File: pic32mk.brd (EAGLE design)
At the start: 110.2 x 85.1 mm, 91 parts, among them IC1 PIC32MK1024MCF100-I_PT, IC10 5.0VDC, IC11 3.3VDC, IC2 ADM3095EBRZ, IC3 TXB0101DCKR, IC4 MAX203ECWP, IC5 TXB0101DCKR, IC6 TXB0101DCKR, IC7 TXB0101DCKR, IC8 TXB0101DCKR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

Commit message: up
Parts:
- added X3: 53261-10, con-molex:53261-10
- moved S1 5.39 mm to (91.4, 10.2)
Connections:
- new net D1+: IC1.57, X3.4
- new net D1-: IC1.56, X3.3
- new net D2+: IC1.60, X3.7
- new net D2-: IC1.59, X3.6
- new net USBID1: IC1.69, X3.1
- new net VBUS: IC1.54, X3.2
- new net VBUS2: IC1.58, X3.5
- net IN7: now also IC1.76; no longer IC1.69
- net SOSCI: now also SPI.10
- net VCC: now also X3.10
- net VDD: now also X3.9; no longer SPI.10
- net VSS: now also X3.8
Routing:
- net VDD: track 439.7 -> 344.6 mm, vias 11 -> 19
- net D2+: track 0.00 -> 70.2 mm, vias 0 -> 3
- net D2-: track 0.00 -> 68.4 mm, vias 0 -> 3
- net VBUS2: track 0.00 -> 63.4 mm, vias 0 -> 3
- net USBID1: track 0.00 -> 60.6 mm, vias 0 -> 2
- net D1-: track 0.00 -> 59.3 mm, vias 0 -> 2
- net D1+: track 0.00 -> 59.3 mm, vias 0 -> 3
- net VBUS: track 0.00 -> 54.8 mm, vias 0 -> 2
- net GND: track 137.7 -> 188.9 mm, vias 4 -> 2
- net RF13: track 96.0 -> 144.4 mm
- net PWM2H: track 86.2 -> 47.9 mm, vias 2 -> 3
- net +24V: track 199.8 -> 237.9 mm, vias 3 -> 5
- net SOSCI: track 0.00 -> 35.4 mm, vias 0 -> 1
- net PWM1L: track 71.6 -> 42.3 mm, vias 2 -> 3
- net RE8: track 62.2 -> 91.1 mm, vias 7 -> 3
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
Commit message: up
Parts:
- renumbered S1 to RESET, X1 to QEI, X3 to USB-BO
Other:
- board text added: "fgb@mchp vcan 1.06"
- board text removed: "fgb@mchp vcan 1.05"

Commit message: up
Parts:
- added QEI3: 22-23-2041, con-molex:22-23-2041
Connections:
- net RG6: now also QEI3.2
- net RG7: now also QEI3.1
- net VDD: now also QEI3.3
- net VSS: now also QEI3.4
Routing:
- net RG7: track 30.8 -> 54.0 mm
- net RG6: track 36.6 -> 50.6 mm
- net RE8: track 91.1 -> 97.3 mm
- net VDD: track 344.6 -> 348.0 mm
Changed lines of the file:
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@@
 <attribute name="VALUE" x="89.59" y="-0.77" size="1.27" layer="27" rot="R180"/>
 </element>
+<element name="QEI3" library="con-molex" library_urn="urn:adsk.eagle:library:165" package="22-23-2041" package3d_urn="urn:adsk.eagle:package:8078635/1" value="22-23-2041" x="7.62" y="36.83" smashed="yes">
+<attribute name="MF" value="MOLEX" x="7.62" y="36.83" size="1.778" layer="27" display="off"/>
+<attribute name="MPN" value="22-23-2041" x="7.62" y="36.83" size="1.778" layer="27" display="off"/>
+<attribute name="NAME" x="2.54" y="40.64" size="1.016" layer="25" ratio="10"/>
+<attribute name="OC_FARNELL" value="1462920" x="7.62" y="36.83" size="1.778" layer="27" display="off"/>
+<attribute name="OC_NEWARK" value="38C0355" x="7.62" y="36.83" size="1.778" layer="27" display="off"/>
+<attribute name="POPULARITY" value="21" x="7.62" y="36.83" size="1.778" layer="27" display="off"/>
+<attribute name="VALUE" x="2.54" y="31.75" size="1.016" layer="27" ratio="10"/>
+</element>
 </elements>
 <signals>
@@
 <wire x1="8.001" y1="46.3296" x2="8.001" y2="51.435" width="0.1524" layer="16"/>
 <wire x1="8.6487" y1="45.6819" x2="8.001" y2="46.3296" width="0.1524" layer="1"/>
-<wire x1="12.3444" y1="41.9862" x2="12.3444" y2="27.8892" width="0.1524" layer="16"/>
-<wire x1="8.001" y1="46.3296" x2="12.3444" y2="41.9862" width="0.1524" layer="16"/>
+<wire x1="12.319" y1="40.7416" x2="8.001" y2="45.0596" width="0.1524" layer="16"/>
+<wire x1="8.001" y1="46.3296" x2="8.001" y2="45.0596" width="0.1524" layer="16"/>
 <wire x1="85.344" y1="33.909" x2="85.1154" y2="33.909" width="0.1524" layer="1"/>
 <wire x1="90.1446" y1="29.1084" x2="85.344" y2="33.909" width="0.1524" layer="1"/>
@@
 <wire x1="9.2202" y1="41.529" x2="10.287" y2="40.4622" width="0.1524" layer="1"/>
 <wire x1="9.2202" y1="41.529" x2="9.21" y2="41.91" width="0.1524" layer="1"/>
+<contactref element="QEI3" pad="3"/>
+<wire x1="9.2964" y1="36.8808" x2="8.9154" y2="36.8808" width="0.1524" layer="16"/>
+<wire x1="11.049" y1="38.6334" x2="9.2964" y2="36.8808" width="0.1524" layer="16"/>
+<wire x1="8.9154" y1="36.8808" x2="8.89" y2="36.83" width="0.1524" layer="16"/>
+<wire x1="11.049" y1="39.4716" x2="11.049" y2="38.6334" width="0.1524" layer="16"/>
+<wire x1="12.319" y1="40.7416" x2="11.049" y2="39.4716" width="0.1524" layer="16"/>
+<wire x1="9.3726" y1="30.861" x2="9.3726" y2="36.8808" width="0.1524" layer="16"/>
+<wire x1="12.3444" y1="27.8892" x2="9.3726" y2="30.861" width="0.1524" layer="16"/>
+<wire x1="9.3726" y1="36.8808" x2="8.89" y2="36.83" width="0.1524" layer="16"/>
 </signal>
 <signal name="VSS" class="1">
@@
 <wire x1="12.6492" y1="46.7106" x2="11.9634" y2="46.7106" width="0.1778" layer="1"/>
 <wire x1="15.7353" y1="49.7967" x2="12.6492" y2="46.7106" width="0.1778" layer="1"/>
+<contactref element="QEI3" pad="4"/>
 </signal>
 <signal name="+5V" class="1">
@@
 <wire x1="14.3256" y1="28.575" x2="15.9258" y2="26.9748" width="0.1524" layer="16"/>
 <wire x1="14.3256" y1="35.052" x2="14.3256" y2="28.575" width="0.1524" layer="16"/>
-<wire x1="7.3152" y1="42.0624" x2="14.3256" y2="35.052" width="0.1524" layer="1"/>
-<wire x1="7.3152" y1="46.5582" x2="7.3152" y2="42.0624" width="0.1524" layer="1"/>
-<wire x1="7.7724" y1="47.0154" x2="7.3152" y2="46.5582" width="0.1524" layer="1"/>
-<wire x1="9.144" y1="47.0154" x2="7.7724" y2="47.0154" width="0.1524" layer="1"/>
+<wire x1="14.3256" y1="35.052" x2="14.3256" y2="37.592" width="0.1524" layer="1"/>
+<wire x1="14.3256" y1="37.592" x2="13.0556" y2="38.862" width="0.1524" layer="1"/>
+<wire x1="13.0556" y1="38.862" x2="6.0452" y2="38.862" width="0.1524" layer="1"/>
+<wire x1="6.0452" y1="47.0154" x2="6.0452" y2="38.862" width="0.1524" layer="1"/>
+<wire x1="9.144" y1="47.0154" x2="6.0452" y2="47.0154" width="0.1524" layer="1"/>
 <wire x1="9.144" y1="47.0154" x2="9.21" y2="46.99" width="0.1524" layer="1"/>
 <via x="19.3548" y="26.8224" extent="1-16" drill="0.35"/>
@@
 <wire x1="1.143" y1="34.0614" x2="1.7526" y2="33.4518" width="0.1524" layer="1"/>
 <wire x1="-1.143" y1="34.0614" x2="1.143" y2="34.0614" width="0.1524" layer="1"/>
-<wire x1="-1.7526" y1="33.4518" x2="-1.143" y2="34.0614" width="0.1524" layer="1"/>
+<wire x1="-1.7526" y1="33.4518" x2="-1.1811" y2="34.0233" width="0.1524" layer="1"/>
+<wire x1="-1.1811" y1="34.0233" x2="-1.143" y2="34.0614" width="0.1524" layer="1"/>
 <wire x1="-1.7526" y1="27.2034" x2="-1.7526" y2="33.4518" width="0.1524" layer="1"/>
 <wire x1="0" y1="25.4508" x2="-1.7526" y2="27.2034" width="0.1524" layer="1"/>
@@
 <wire x1="1.7526" y1="33.4518" x2="18.0594" y2="33.4518" width="0.1524" layer="1"/>
 <wire x1="23.6982" y1="29.1846" x2="23.742" y2="29.14" width="0.1524" layer="1"/>
+<contactref element="QEI3" pad="2"/>
+<wire x1="5.9436" y1="36.8808" x2="6.3246" y2="36.8808" width="0.1524" layer="1"/>
+<wire x1="3.7338" y1="39.0906" x2="5.9436" y2="36.8808" width="0.1524" layer="1"/>
+<wire x1="-1.2192" y1="39.0906" x2="3.7338" y2="39.0906" width="0.1524" layer="1"/>
+<wire x1="-1.7526" y1="38.5572" x2="-1.2192" y2="39.0906" width="0.1524" layer="1"/>
+<wire x1="-1.7526" y1="34.5948" x2="-1.7526" y2="38.5572" width="0.1524" layer="1"/>
+<wire x1="-1.1811" y1="34.0233" x2="-1.7526" y2="34.5948" width="0.1524" layer="1"/>
+<wire x1="6.3246" y1="36.8808" x2="6.35" y2="36.83" width="0.1524" layer="1"/>
 </signal>
 <signal name="RG7">
@@
 <via x="25.0698" y="28.2702" extent="1-15" drill="0.35"/>
 <via x="20.8026" y="24.2316" extent="1-16" drill="0.35"/>
+<contactref element="QEI3" pad="1"/>
+<wire x1="3.81" y1="39.0144" x2="3.81" y2="36.83" width="0.1524" layer="16"/>
+<wire x1="1.143" y1="41.6814" x2="3.81" y2="39.0144" width="0.1524" layer="16"/>
+<wire x1="-1.143" y1="41.6814" x2="1.143" y2="41.6814" width="0.1524" layer="16"/>
+<wire x1="-2.0574" y1="40.767" x2="-1.143" y2="41.6814" width="0.1524" layer="16"/>
+<wire x1="-2.0574" y1="30.0228" x2="-2.0574" y2="40.767" width="0.1524" layer="16"/>
+<wire x1="0" y1="27.9654" x2="-2.0574" y2="30.0228" width="0.1524" layer="16"/>
+<wire x1="0" y1="27.9654" x2="0" y2="27.94" width="0.1524" layer="16"/>
 </signal>
 <signal name="RG8">

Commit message: up
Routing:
- net VDD: track 348.0 -> 398.4 mm, vias 19 -> 17
- net GND: track 188.9 -> 148.6 mm, vias 2 -> 4
- net VSS: track 404.4 -> 443.3 mm
- net +24V: track 237.9 -> 199.3 mm, vias 5 -> 3
- net RG15: track 116.1 -> 147.4 mm, vias 6 -> 4
- net U202: track 60.9 -> 34.8 mm, vias 0 -> 1
- net RPA14: track 38.4 -> 62.1 mm, vias 3 -> 0
- net RG7: track 54.0 -> 33.6 mm, vias 2 -> 1
- net U2RX: track 83.6 -> 100.7 mm, vias 3 -> 2
- net VCC: track 324.8 -> 341.7 mm, vias 5 -> 4
- net RG6: track 50.6 -> 34.6 mm
- net REFOUT: track 101.3 -> 85.6 mm
- net PWM4L: track 59.8 -> 73.8 mm
- net MCLEAR: track 136.5 -> 150.4 mm, vias 3 -> 6
- net SCK3: track 24.2 -> 38.1 mm
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
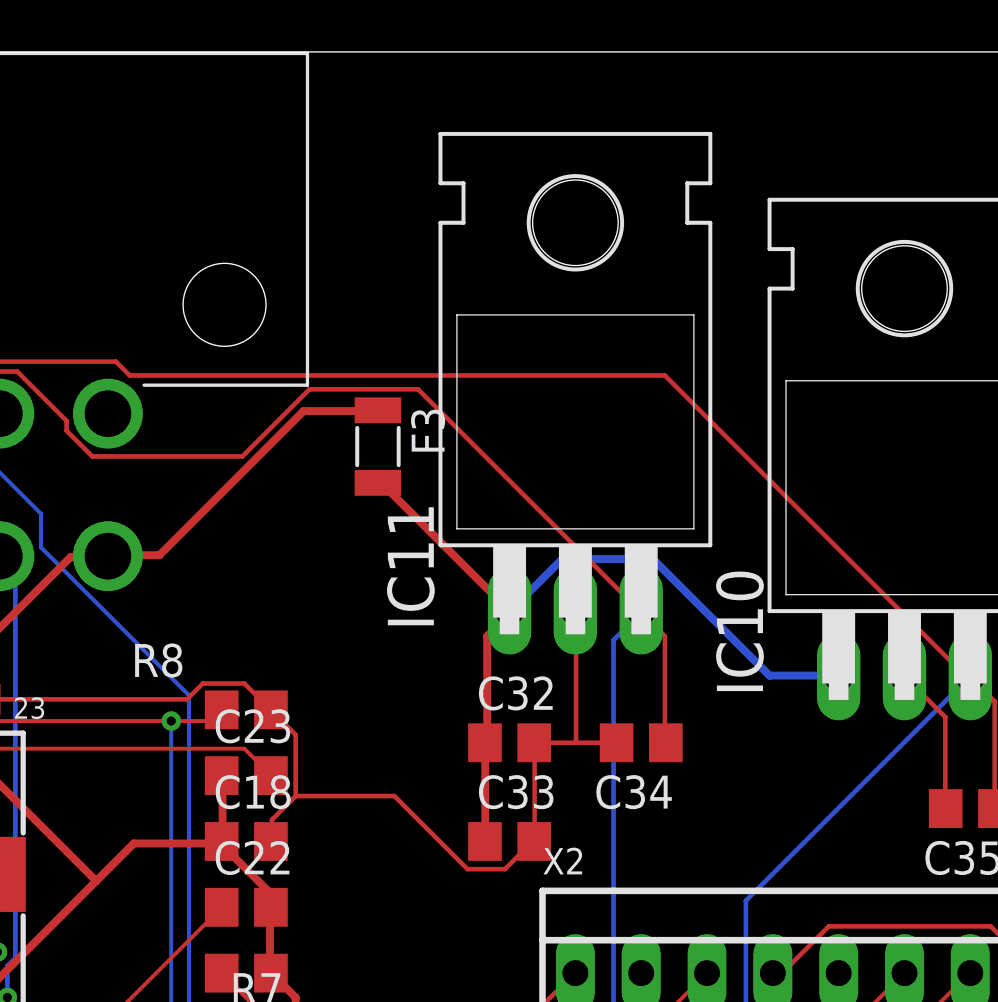
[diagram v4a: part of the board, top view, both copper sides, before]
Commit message: add bulk caps
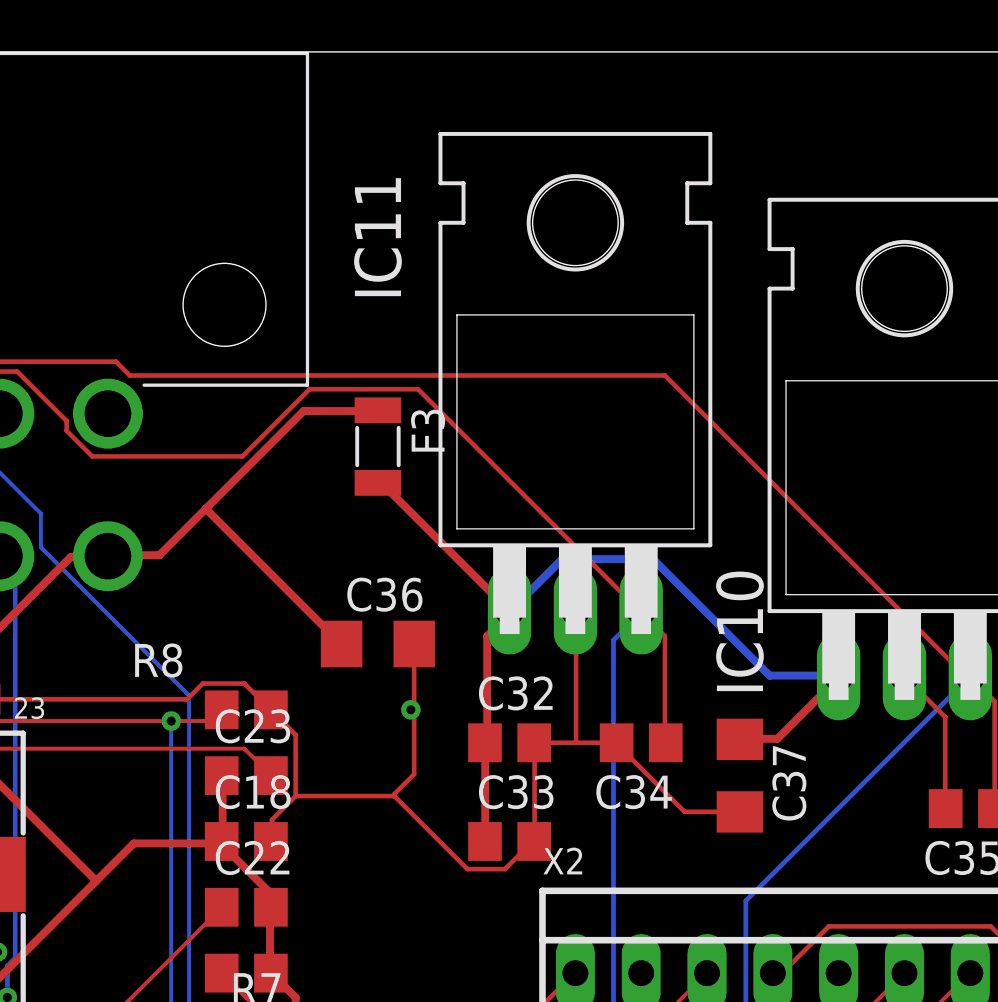
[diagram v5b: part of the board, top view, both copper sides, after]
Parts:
- added C36, C37: 10uf, rcl:C1206
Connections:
- net +24V: now also C36.1
- net N$30: now also C37.1
- net VSS: now also C36.2, C37.2
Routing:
- net VSS: track 443.3 -> 455.4 mm, vias 12 -> 13
- net +24V: track 199.3 -> 206.7 mm
- net N$30: track 31.9 -> 36.7 mm
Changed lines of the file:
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@@
 </element>
 <element name="IC11" library="linear" library_urn="urn:adsk.eagle:library:262" package="TO220H" package3d_urn="urn:adsk.eagle:package:16414/1" value="3.3VDC" x="85.09" y="68.58" smashed="yes">
-<attribute name="NAME" x="79.629" y="57.658" size="1.778" layer="25" ratio="10" rot="R90"/>
+<attribute name="NAME" x="78.359" y="70.358" size="1.778" layer="25" ratio="10" rot="R90"/>
 <attribute name="POPULARITY" value="35" x="85.09" y="68.58" size="1.778" layer="27" display="off"/>
 <attribute name="VALUE" x="92.456" y="57.531" size="1.778" layer="27" ratio="10" rot="R90"/>
@@
 <attribute name="VALUE" x="2.54" y="31.75" size="1.016" layer="27" ratio="10"/>
 </element>
+<element name="C36" library="rcl" library_urn="urn:adsk.eagle:library:334" package="C1206" package3d_urn="urn:adsk.eagle:package:23618/2" value="10uf" x="77.47" y="57.15" smashed="yes">
+<attribute name="NAME" x="76.2" y="58.42" size="1.27" layer="25"/>
+<attribute name="POPULARITY" value="24" x="77.47" y="57.15" size="1.778" layer="27" display="off"/>
+<attribute name="SPICEPREFIX" value="C" x="77.47" y="57.15" size="1.778" layer="27" display="off"/>
+<attribute name="VALUE" x="76.2" y="54.61" size="1.27" layer="27"/>
+</element>
+<element name="C37" library="rcl" library_urn="urn:adsk.eagle:library:334" package="C1206" package3d_urn="urn:adsk.eagle:package:23618/2" value="10uf" x="91.44" y="52.07" smashed="yes" rot="R270">
+<attribute name="NAME" x="92.71" y="53.34" size="1.27" layer="25" rot="R270"/>
+<attribute name="POPULARITY" value="24" x="91.44" y="52.07" size="1.778" layer="27" rot="R270" display="off"/>
+<attribute name="SPICEPREFIX" value="C" x="91.44" y="52.07" size="1.778" layer="27" rot="R270" display="off"/>
+<attribute name="VALUE" x="88.9" y="53.34" size="1.27" layer="27" rot="R270"/>
+</element>
 </elements>
 <signals>
@@
 <wire x1="11.6586" y1="46.9392" x2="11.2014" y2="46.9392" width="0.1778" layer="1"/>
 <wire x1="11.2014" y1="46.9392" x2="11.11" y2="46.99" width="0.1778" layer="1"/>
+<contactref element="C36" pad="2"/>
+<contactref element="C37" pad="2"/>
+<wire x1="78.867" y1="52.1208" x2="78.867" y2="57.15" width="0.1778" layer="1"/>
+<wire x1="78.105" y1="51.3588" x2="78.867" y2="52.1208" width="0.1778" layer="1"/>
+<wire x1="78.867" y1="57.15" x2="78.87" y2="57.15" width="0.1778" layer="1"/>
+<wire x1="78.105" y1="51.3588" x2="78.105" y2="51.2826" width="0.1778" layer="1"/>
+<wire x1="89.3064" y1="50.673" x2="91.44" y2="50.673" width="0.1778" layer="1"/>
+<wire x1="86.7156" y1="53.2638" x2="89.3064" y2="50.673" width="0.1778" layer="1"/>
+<wire x1="91.44" y1="50.673" x2="91.44" y2="50.67" width="0.1778" layer="1"/>
+<wire x1="86.7156" y1="53.2638" x2="86.68" y2="53.34" width="0.1778" layer="1"/>
+<via x="78.74" y="54.61" extent="1-2" drill="0.35"/>
 </signal>
 <signal name="+5V" class="1">
@@
 <wire x1="65.0748" y1="37.1094" x2="65.005" y2="37.23" width="0.3048" layer="1"/>
 <wire x1="74.5998" y1="66.1416" x2="77.4192" y2="66.1416" width="0.3048" layer="1"/>
-<wire x1="69.0372" y1="60.579" x2="74.5998" y2="66.1416" width="0.3048" layer="1"/>
+<wire x1="69.0372" y1="60.579" x2="70.8279" y2="62.3697" width="0.3048" layer="1"/>
+<wire x1="70.8279" y1="62.3697" x2="74.5998" y2="66.1416" width="0.3048" layer="1"/>
 <wire x1="67.056" y1="60.579" x2="69.0372" y2="60.579" width="0.3048" layer="1"/>
 <wire x1="77.4192" y1="66.1416" x2="77.47" y2="66.17" width="0.3048" layer="1"/>
@@
 <via x="58.3692" y="39.3954" extent="1-16" drill="0.35"/>
 <via x="63.8556" y="25.6032" extent="1-16" drill="0.35"/>
+<contactref element="C36" pad="1"/>
+<wire x1="70.8279" y1="62.3697" x2="76.0476" y2="57.15" width="0.3048" layer="1"/>
+<wire x1="76.0476" y1="57.15" x2="76.07" y2="57.15" width="0.3048" layer="1"/>
 </signal>
 <signal name="RPB1">
@@
 <wire x1="95.25" y1="55.9308" x2="95.25" y2="55.88" width="0.3048" layer="16"/>
 <wire x1="82.6008" y1="58.4454" x2="82.55" y2="58.42" width="0.3048" layer="16"/>
+<contactref element="C37" pad="1"/>
+<wire x1="92.8878" y1="53.4924" x2="91.44" y2="53.4924" width="0.3048" layer="1"/>
+<wire x1="95.25" y1="55.8546" x2="92.8878" y2="53.4924" width="0.3048" layer="1"/>
+<wire x1="91.44" y1="53.4924" x2="91.44" y2="53.47" width="0.3048" layer="1"/>
+<wire x1="95.25" y1="55.8546" x2="95.25" y2="55.88" width="0.3048" layer="1"/>
 </signal>
 <signal name="USBID1">

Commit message: add switch code
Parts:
- U4: value REF3440IDBVR -> REF3425IDBVR
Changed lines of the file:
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@@
 <layer number="25" name="tNames" color="7" fill="1" visible="yes" active="yes"/>
 <layer number="26" name="bNames" color="7" fill="1" visible="yes" active="yes"/>
-<layer number="27" name="tValues" color="7" fill="1" visible="no" active="yes"/>
+<layer number="27" name="tValues" color="7" fill="1" visible="yes" active="yes"/>
 <layer number="28" name="bValues" color="7" fill="1" visible="no" active="yes"/>
 <layer number="29" name="tStop" color="7" fill="3" visible="no" active="yes"/>
@@
 <attribute name="VALUE" x="3.175" y="3.81" size="1.27" layer="27" rot="R90"/>
 </element>
-<element name="U4" library="REF3440IDBVR" package="SOT95P280X145-6N" value="REF3440IDBVR" x="10.16" y="24.13" smashed="yes">
+<element name="U4" library="REF3440IDBVR" package="SOT95P280X145-6N" value="REF3425IDBVR" x="10.16" y="24.13" smashed="yes">
 <attribute name="AVAILABILITY" value="Unavailable" x="10.16" y="24.13" size="1.778" layer="27" display="off"/>
 <attribute name="DESCRIPTION" value=" Series Voltage Reference IC ±0.05% SOT-23-6 " x="10.16" y="24.13" size="1.778" layer="27" display="off"/>
@@
 <attribute name="NAME" x="92.329" y="55.118" size="1.778" layer="25" ratio="10" rot="R90"/>
 <attribute name="POPULARITY" value="35" x="97.79" y="66.04" size="1.778" layer="27" display="off"/>
-<attribute name="VALUE" x="105.156" y="54.991" size="1.778" layer="27" ratio="10" rot="R90"/>
+<attribute name="VALUE" x="105.156" y="62.611" size="1.778" layer="27" ratio="10" rot="R90"/>
 </element>
 <element name="IC11" library="linear" library_urn="urn:adsk.eagle:library:262" package="TO220H" package3d_urn="urn:adsk.eagle:package:16414/1" value="3.3VDC" x="85.09" y="68.58" smashed="yes">
 <attribute name="NAME" x="78.359" y="70.358" size="1.778" layer="25" ratio="10" rot="R90"/>
 <attribute name="POPULARITY" value="35" x="85.09" y="68.58" size="1.778" layer="27" display="off"/>
-<attribute name="VALUE" x="92.456" y="57.531" size="1.778" layer="27" ratio="10" rot="R90"/>
+<attribute name="VALUE" x="92.456" y="62.611" size="1.778" layer="27" ratio="10" rot="R90"/>
 </element>
 <element name="C32" library="rcl" library_urn="urn:adsk.eagle:library:334" package="C0805" package3d_urn="urn:adsk.eagle:package:23617/2" value="0.1" x="82.55" y="53.34" smashed="yes">

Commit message: up
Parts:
- added C38, C39, C42, C43, C44, C45: 0.1, rcl:C0805
- added C40, C41, C46: 10uf, rcl:C1206
- moved C36 1.27 mm to (77.5, 55.9), turned to 90 degrees
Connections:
- net +24V: now also C38.2, C39.2, C40.1, C41.1, C42.1, C43.1, C44.1, C45.1, C46.1
- net VSS: now also C38.1, C39.1, C40.2, C41.2, C42.2, C43.2, C44.2, C45.2, C46.2
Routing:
- net +24V: track 206.7 -> 266.9 mm, vias 3 -> 9
- net RF13: track 150.1 -> 101.5 mm
- net GND: track 148.6 -> 195.8 mm, vias 4 -> 3
- net RG15: track 147.4 -> 102.5 mm
- net SCK3: track 38.1 -> 76.2 mm, vias 1 -> 0
- net U204: track 53.5 -> 88.2 mm
- net MCLEAR: track 150.4 -> 183.6 mm, vias 6 -> 1
- net +5V: track 198.7 -> 227.2 mm
- net U2RX: track 100.7 -> 75.8 mm
- net RE14: track 73.2 -> 97.0 mm, vias 2 -> 3
- net N$41: track 13.2 -> 36.2 mm
- net VCC: track 341.7 -> 318.9 mm
- net RG6: track 34.6 -> 54.5 mm, vias 0 -> 1
- net PWM4L: track 73.8 -> 56.1 mm
- net RPA14: track 62.1 -> 45.9 mm, vias 0 -> 3
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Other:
- board text added: "fgb@mchp vcan 1.07"
- board text removed: "fgb@mchp vcan 1.06"

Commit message: up
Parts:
- added C47: 0.1, rcl:C0805
- added C48: 10uf, rcl:C1206
- added QEI_VOLTS: 1-2 3.3, 3-2 5.0, con-lstb:MA03-1
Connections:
- new net N$28: QEI.7, QEI.8, QEI_VOLTS.2
- net +24V: now also C47.1, C48.1
- net GND: now also C47.2, C48.2
- net VCC: now also QEI_VOLTS.3; no longer QEI.7, QEI.8
- net VDD: now also QEI_VOLTS.1
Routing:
- net N$28: track 0.00 -> 29.7 mm
- net GND: track 195.8 -> 202.9 mm, vias 3 -> 4
- net VDD: track 384.2 -> 389.9 mm
- net +24V: track 266.9 -> 270.6 mm
- net VCC: track 318.9 -> 322.0 mm
